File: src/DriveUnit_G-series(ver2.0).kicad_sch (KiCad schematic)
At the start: 53 parts, among them IC1 A3921, Q10 SQJA16EP-T1_GE3, Q5 Q_NPN_BCE, Q6 Q_NPN_BCE, SW3 THAF01-NC-R, U21 TC7S14F

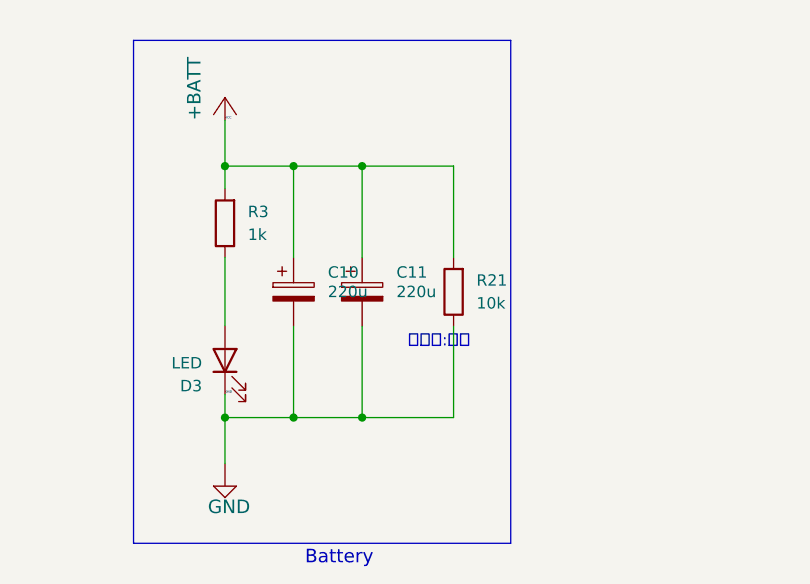
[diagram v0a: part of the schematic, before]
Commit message: [complete]配線完了
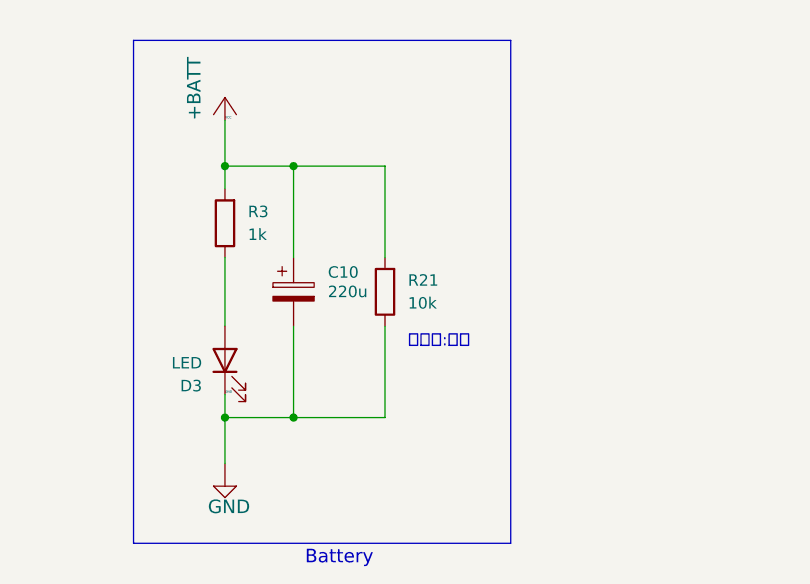
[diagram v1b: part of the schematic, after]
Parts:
- removed C11: 220u, Symbol:U2-R_NCH, symbol Device:C_Polarized
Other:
- moved on the sheet: R21
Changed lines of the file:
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@@
   (junction (at 53.34 43.18) (diameter 0) (color 0 0 0 0)
   )
-  (junction (at 345.44 190.5) (diameter 0) (color 0 0 0 0)
-  )
   (junction (at 295.91 66.04) (diameter 0) (color 0 0 0 0)
   )
@@
   (junction (at 53.34 45.72) (diameter 0) (color 0 0 0 0)
   )
-  (junction (at 345.44 218.44) (diameter 0) (color 0 0 0 0)
-  )
   (junction (at 330.2 218.44) (diameter 0) (color 0 0 0 0)
   )
@@
     (stroke (width 0) (type default))
   )
-  (wire (pts (xy 345.44 218.44) (xy 337.82 218.44))
+  (wire (pts (xy 337.82 218.44) (xy 347.98 218.44))
     (stroke (width 0) (type default))
   )
@@
     (stroke (width 0) (type default))
   )
-  (wire (pts (xy 355.6 208.28) (xy 355.6 218.44))
+  (wire (pts (xy 347.98 208.28) (xy 347.98 218.44))
     (stroke (width 0) (type default))
   )
@@
     (stroke (width 0) (type default))
   )
-  (wire (pts (xy 345.44 208.28) (xy 345.44 218.44))
-    (stroke (width 0) (type default))
-  )
   (polyline (pts (xy 302.26 175.26) (xy 279.4 175.26))
     (stroke (width 0) (type solid))
@@
     (stroke (width 0) (type default))
   )
-  (wire (pts (xy 345.44 190.5) (xy 345.44 200.66))
-    (stroke (width 0) (type default))
-  )
   (wire (pts (xy 281.94 121.92) (xy 281.94 116.84))
     (stroke (width 0) (type default))
@@
     (stroke (width 0) (type default))
   )
-  (wire (pts (xy 355.6 200.66) (xy 355.6 190.5))
+  (wire (pts (xy 347.98 200.66) (xy 347.98 190.5))
     (stroke (width 0) (type default))
   )
@@
     (stroke (width 0) (type solid))
   )
-  (wire (pts (xy 337.82 190.5) (xy 345.44 190.5))
+  (wire (pts (xy 337.82 190.5) (xy 347.98 190.5))
     (stroke (width 0) (type default))
   )
@@
     (stroke (width 0) (type default))
   )
-  (wire (pts (xy 355.6 218.44) (xy 345.44 218.44))
-    (stroke (width 0) (type default))
-  )
   (wire (pts (xy 281.94 81.28) (xy 279.4 81.28))
     (stroke (width 0) (type default))
@@
     (stroke (width 0) (type default))
   )
-  (wire (pts (xy 355.6 190.5) (xy 345.44 190.5))
-    (stroke (width 0) (type default))
-  )
   (wire (pts (xy 194.31 151.13) (xy 207.01 151.13))
     (stroke (width 0) (type default))
@@
     )
   )
-  (symbol (lib_id "Device:C_Polarized") (at 345.44 204.47 0) (unit 1)
-    (in_bom yes) (on_board yes) (dnp no)
-    (property "Reference" "C11" (at 349.25 202.311 0)
-      (effects (font (size 1.27 1.27)) (justify left))
-    )
-    (property "Value" "220u" (at 349.25 204.47 0)
-      (effects (font (size 1.27 1.27)) (justify left))
-    )
-    (property "Footprint" "Symbol:U2-R_NCH" (at 346.4052 208.28 0)
-      (effects (font (size 1.27 1.27)) hide)
-    )
-    (property "Datasheet" "~" (at 345.44 204.47 0)
-      (effects (font (size 1.27 1.27)) hide)
-    )
-    (pin "1")
-    (pin "2")
-    (instances
-      (project "DriveUnit_G-series(ver2.0)"
-        (path "/a976a501-1e7b-4c4e-8f61-f1c2917a0bf3"
-          (reference "C11") (unit 1)
-        )
-      )
-    )
-  )
   (symbol (lib_id "(Eagle)PowerUnit-Bseries(ver2.0)-eagle-import:V2P22LHM3/H") (at 331.47 83.82 90) (unit 1)
     (in_bom yes) (on_board yes) (dnp no)
@@
     )
   )
-  (symbol (lib_id "Device:R") (at 355.6 204.47 180) (unit 1)
+  (symbol (lib_id "Device:R") (at 347.98 204.47 180) (unit 1)
     (in_bom yes) (on_board yes) (dnp no)
-    (property "Reference" "R21" (at 358.14 203.2 0)
+    (property "Reference" "R21" (at 350.52 203.2 0)
       (effects (font (size 1.27 1.27)) (justify right))
     )
-    (property "Value" "10k" (at 358.14 205.74 0)
+    (property "Value" "10k" (at 350.52 205.74 0)
       (effects (font (size 1.27 1.27)) (justify right))
     )
-    (property "Footprint" "Resistor_SMD:R_0603_1608Metric_Pad0.98x0.95mm_HandSolder" (at 357.378 204.47 90)
+    (property "Footprint" "Resistor_SMD:R_0603_1608Metric_Pad0.98x0.95mm_HandSolder" (at 349.758 204.47 90)
       (effects (font (size 1.27 1.27)) hide)
     )
-    (property "Datasheet" "~" (at 355.6 204.47 0)
+    (property "Datasheet" "~" (at 347.98 204.47 0)
       (effects (font (size 1.27 1.27)) hide)
     )
